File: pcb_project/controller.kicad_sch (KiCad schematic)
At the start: 4 parts, among them U3 COM-09032, U4 COM-09032

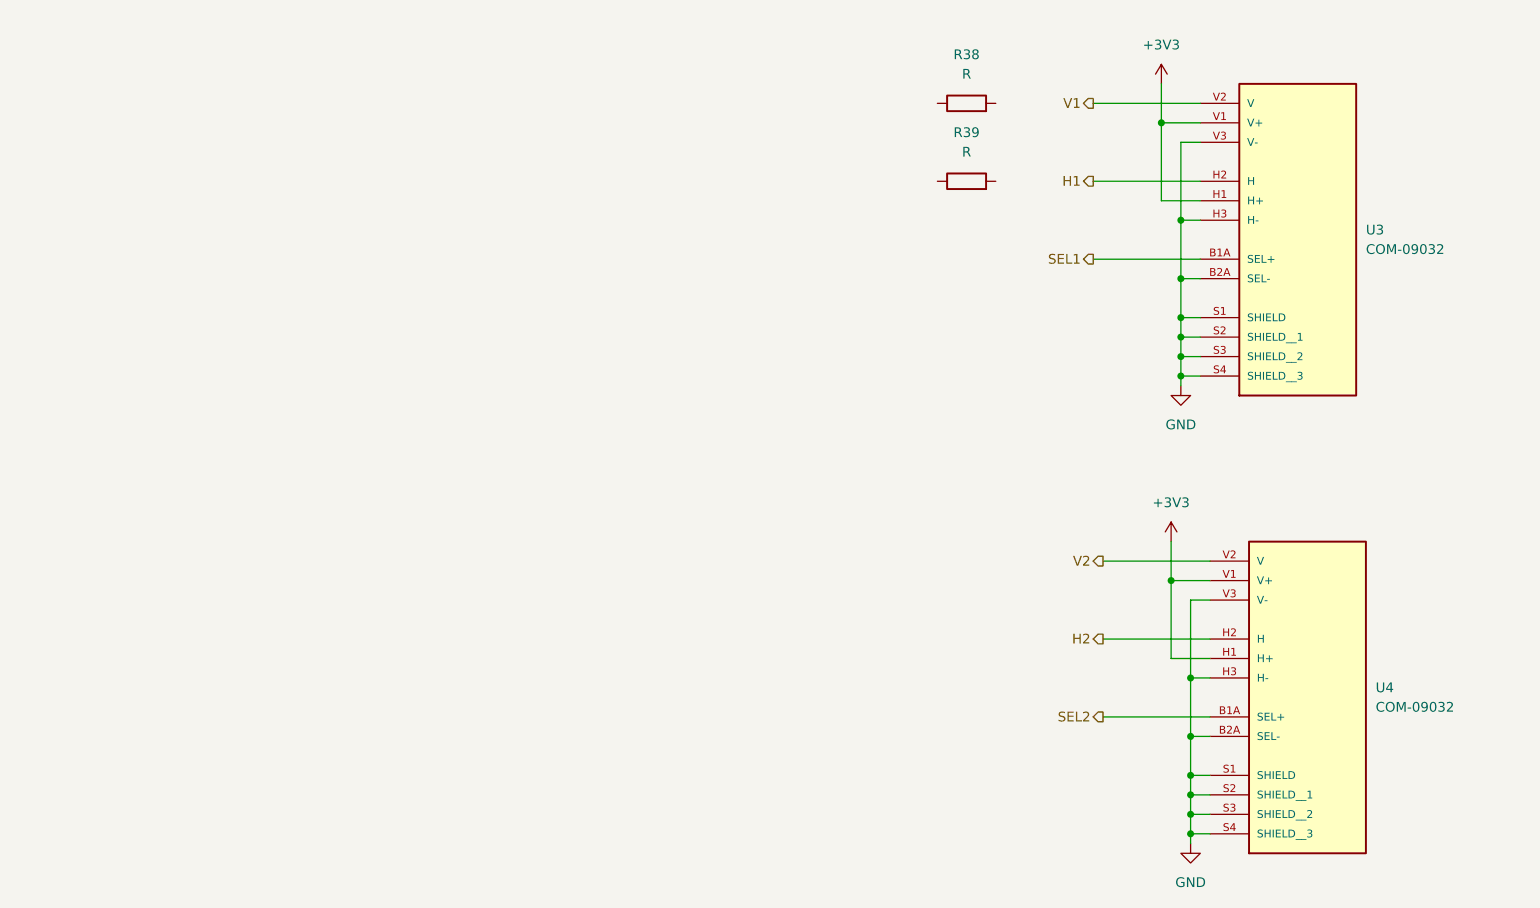
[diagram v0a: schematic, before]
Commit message: Add button symbol
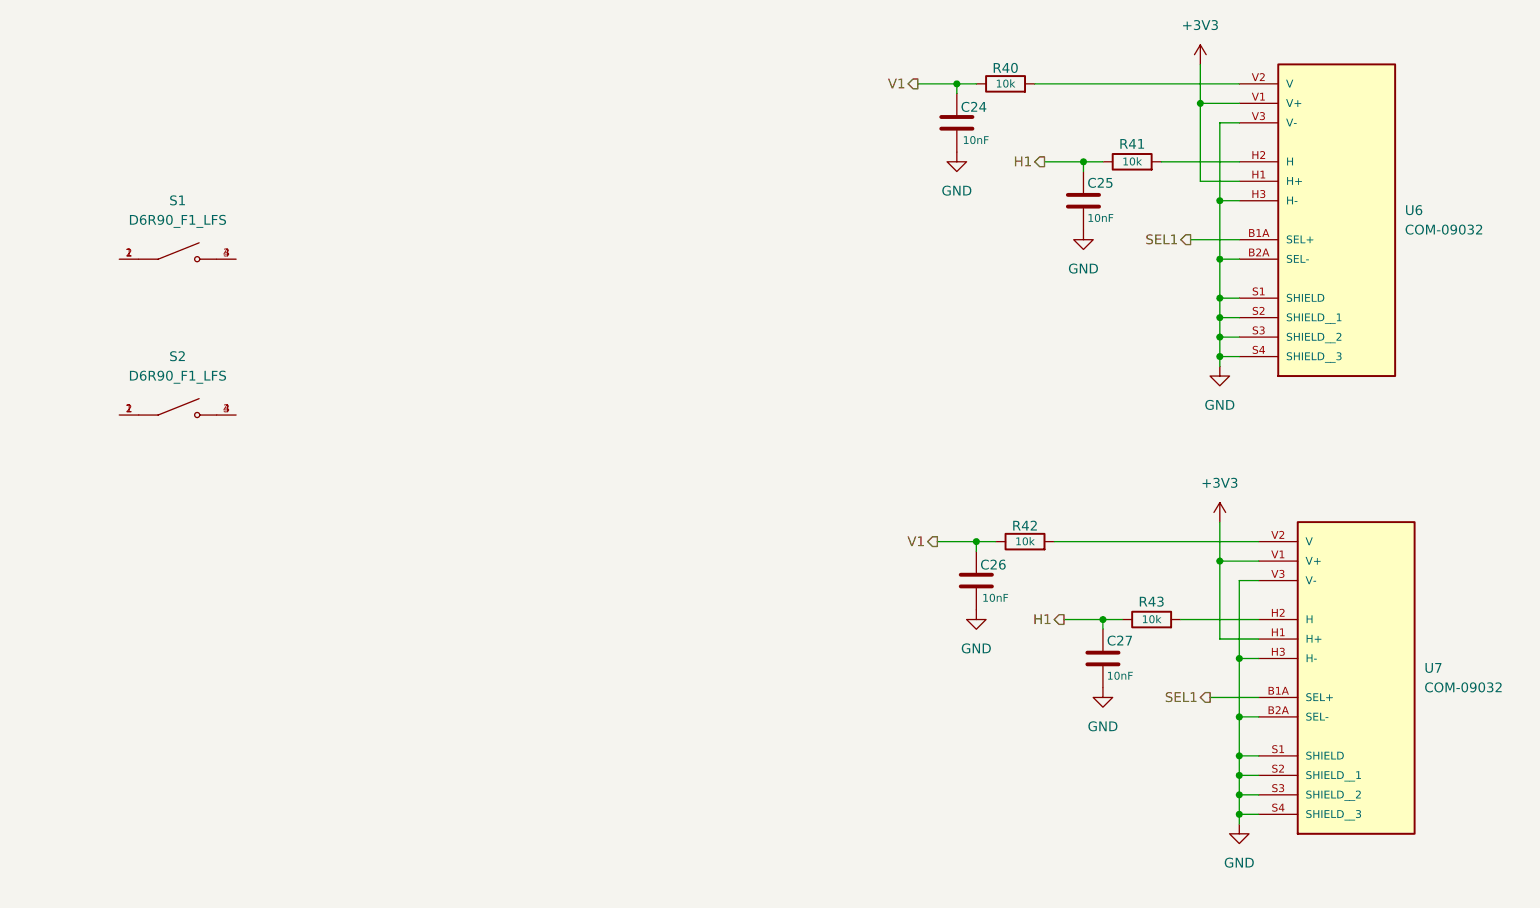
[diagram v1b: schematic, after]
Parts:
- removed R38, R39: R, symbol Device:R
- removed U3, U4: COM-09032, COM-09032:XDCR_COM-09032, symbol COM-09032:COM-09032
- added C24, C25, C26, C27: 10nF, symbol Device:C
- added R40, R41, R42, R43: 10k, symbol Device:R
- added S1, S2: D6R90_F1_LFS, D6R90_F1_LFS:SW_D6R90_F1_LFS, symbol D6R90_F1_LFS:D6R90_F1_LFS
- added U6, U7: COM-09032, COM-09032:XDCR_COM-09032, symbol COM-09032:COM-09032
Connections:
- net +3V3: now also U6.H1 (H+), U6.V1 (V+), U7.H1 (H+), U7.V1 (V+)
- net GND: now also C24.2, C25.2, C26.2, C27.2, U6.B2A (SEL-), U6.H3 (H-), U6.S1 (SHIELD), U6.S2 (SHIELD__1), U6.S3 (SHIELD__2), U6.S4 (SHIELD__3), U6.V3 (V-), U7.B2A (SEL-), U7.H3 (H-), U7.S1 (SHIELD), U7.S2 (SHIELD__1), U7.S3 (SHIELD__2), U7.S4 (SHIELD__3), U7.V3 (V-)
- net H1: now also C25.1, C27.1, R41.1, R43.1
- net SEL1: now also U6.B1A (SEL+), U7.B1A (SEL+)
- net V1: now also C24.1, C26.1, R40.1, R42.1
- new net: R41.2, U6.H2 (H)
- new net: R40.2, U6.V2 (V)
- new net: S2.1, S2.2
- new net: S2.3, S2.4
- new net: R43.2, U7.H2 (H)
- new net: R42.2, U7.V2 (V)
- new net: S1.1, S1.2
- new net: S1.3, S1.4

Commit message: Finish controller schema
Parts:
- removed U7: COM-09032, COM-09032:XDCR_COM-09032, symbol COM-09032:COM-09032
- added R38, R39, R44, R45: 10k, symbol Device:R
- added U3: COM-09032, COM-09032:XDCR_COM-09032, symbol COM-09032:COM-09032
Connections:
- net +3V3: now also R38.1, R39.1, R44.1, R45.1, U3.H1 (H+), U3.V1 (V+)
- net GND: now also S1.1, S1.2, S2.1, S2.2, U3.B2A (SEL-), U3.H3 (H-), U3.S1 (SHIELD), U3.S2 (SHIELD__1), U3.S3 (SHIELD__2), U3.S4 (SHIELD__3), U3.V3 (V-)
- net H1: no longer C27.1, R43.1
- net SEL1: now also R44.2
- net V1: no longer C26.1, R42.1
- net B2: now reaches S2.3, S2.4
- net B2: now also R39.2
- net at R43.2: now also U3.H2 (H)
- net at R42.2: now also U3.V2 (V)
- net B1: now reaches S1.3, S1.4
- net B1: now also R38.2
- new net H2: C27.1, R43.1
- new net SEL2: R45.2, U3.B1A (SEL+)
- new net V2: C26.1, R42.1
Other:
- moved on the sheet: C24, C25, R40, R41, S1, U6

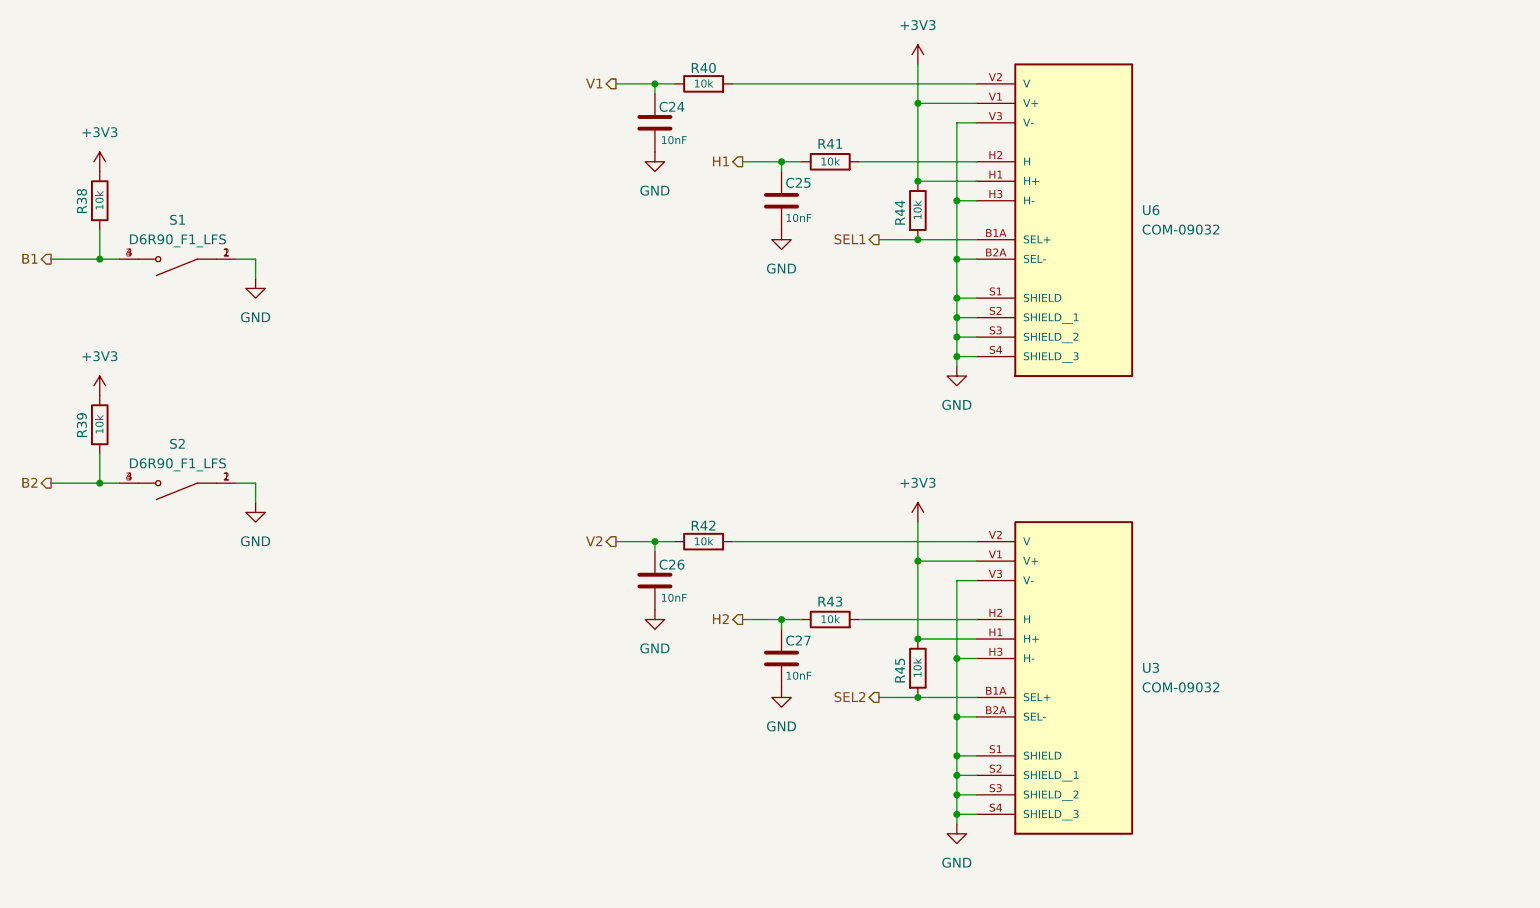
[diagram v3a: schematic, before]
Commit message: ERC fixes, some remain
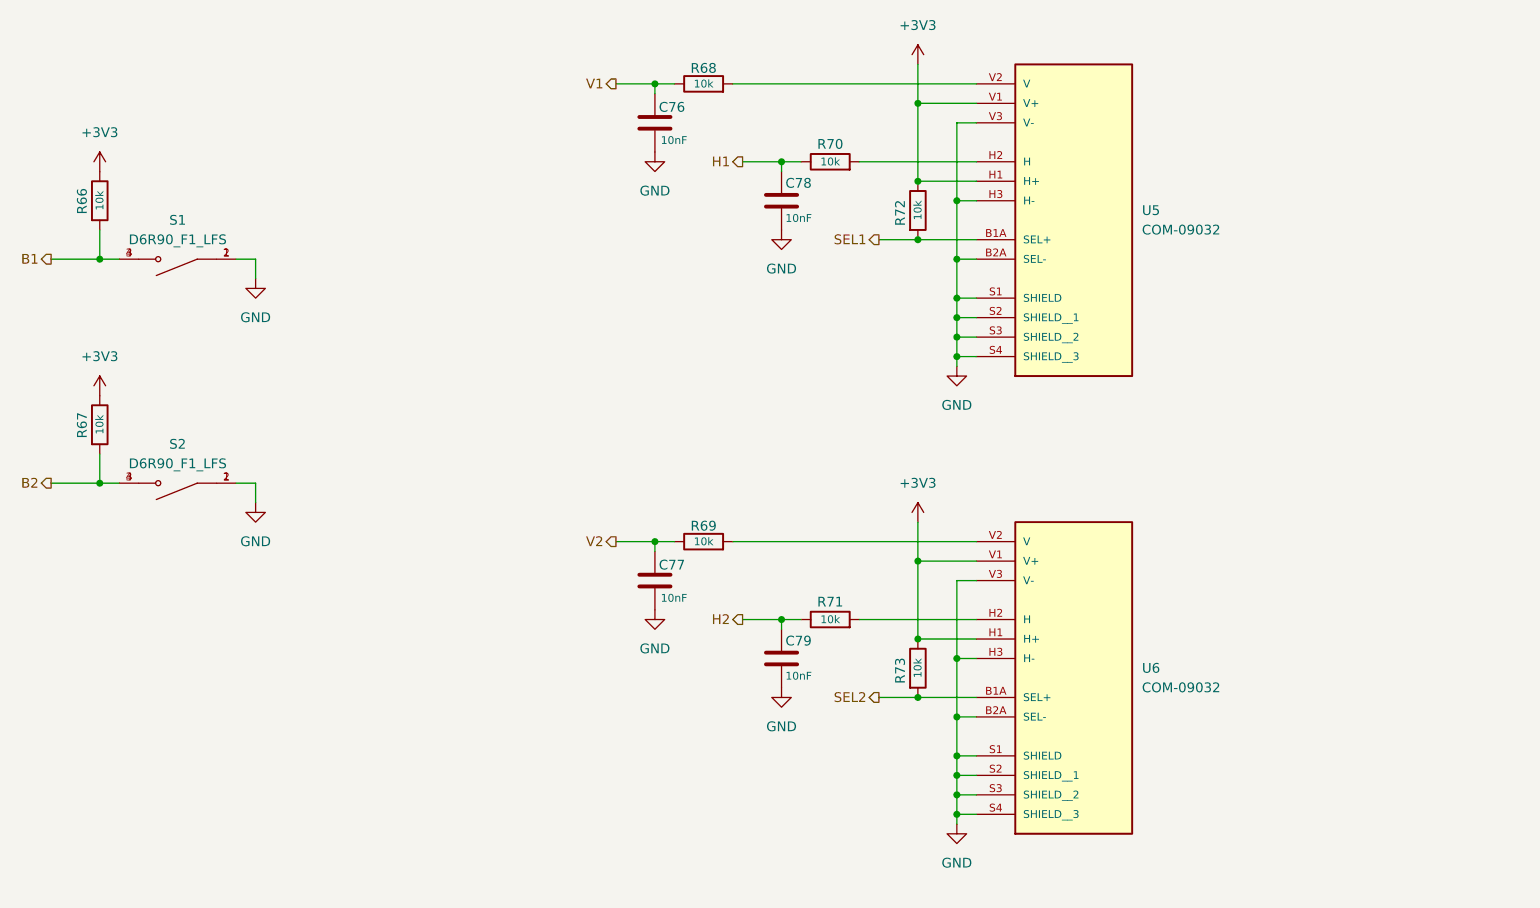
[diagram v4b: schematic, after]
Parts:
- renumbered C24 to C76, C26 to C77, C25 to C78, C27 to C79, R38 to R66, R39 to R67, R40 to R68, R42 to R69, R41 to R70, R43 to R71, R44 to R72, R45 to R73, U6 to U5, U3 to U6
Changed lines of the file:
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@@
 		(dnp no)
 		(fields_autoplaced yes)
-		(property "Reference" "#PWR018"
+		(property "Reference" "#PWR085"
 			(at 82.55 55.88 0)
 			(effects
@@
 			(project ""
 				(path "/98f80f66-4595-4d0f-90ca-59b2db6f447b/8d37cb1b-68e3-4c4f-bec3-1efbc6c7e4dc"
-					(reference "#PWR018")
+					(reference "#PWR085")
 					(unit 1)
 				)
@@
 		(on_board yes)
 		(dnp no)
-		(property "Reference" "R43"
+		(property "Reference" "R71"
 			(at 177.8 108.204 90)
 			(effects
@@
 			(project "pcb_project"
 				(path "/98f80f66-4595-4d0f-90ca-59b2db6f447b/8d37cb1b-68e3-4c4f-bec3-1efbc6c7e4dc"
-					(reference "R43")
+					(reference "R71")
 					(unit 1)
 				)
@@
 		(on_board yes)
 		(dnp no)
-		(property "Reference" "U6"
+		(property "Reference" "U5"
 			(at 218.44 57.1499 0)
 			(effects
@@
 			(project "pcb_project"
 				(path "/98f80f66-4595-4d0f-90ca-59b2db6f447b/8d37cb1b-68e3-4c4f-bec3-1efbc6c7e4dc"
-					(reference "U6")
+					(reference "U5")
 					(unit 1)
 				)
@@
 		(dnp no)
 		(fields_autoplaced yes)
-		(property "Reference" "#PWR016"
+		(property "Reference" "#PWR087"
 			(at 102.87 72.39 0)
 			(effects
@@
 			(project ""
 				(path "/98f80f66-4595-4d0f-90ca-59b2db6f447b/8d37cb1b-68e3-4c4f-bec3-1efbc6c7e4dc"
-					(reference "#PWR016")
+					(reference "#PWR087")
 					(unit 1)
 				)
@@
 		(on_board yes)
 		(dnp no)
-		(property "Reference" "U3"
+		(property "Reference" "U6"
 			(at 218.44 116.8399 0)
 			(effects
@@
 			(project "pcb_project"
 				(path "/98f80f66-4595-4d0f-90ca-59b2db6f447b/8d37cb1b-68e3-4c4f-bec3-1efbc6c7e4dc"
-					(reference "U3")
+					(reference "U6")
 					(unit 1)
 				)
@@
 		(dnp no)
 		(fields_autoplaced yes)
-		(property "Reference" "#PWR025"
+		(property "Reference" "#PWR094"
 			(at 189.23 101.6 0)
 			(effects
@@
 			(project "pcb_project"
 				(path "/98f80f66-4595-4d0f-90ca-59b2db6f447b/8d37cb1b-68e3-4c4f-bec3-1efbc6c7e4dc"
-					(reference "#PWR025")
+					(reference "#PWR094")
 					(unit 1)
 				)
@@
 		(dnp no)
 		(fields_autoplaced yes)
-		(property "Reference" "#PWR0110"
+		(property "Reference" "#PWR092"
 			(at 171.45 125.73 0)
 			(effects
@@
 			(project "pcb_project"
 				(path "/98f80f66-4595-4d0f-90ca-59b2db6f447b/8d37cb1b-68e3-4c4f-bec3-1efbc6c7e4dc"
-					(reference "#PWR0110")
+					(reference "#PWR092")
 					(unit 1)
 				)
@@
 		(dnp no)
 		(fields_autoplaced yes)
-		(property "Reference" "#PWR022"
+		(property "Reference" "#PWR095"
 			(at 194.31 83.82 0)
 			(effects
@@
 			(project "pcb_project"
 				(path "/98f80f66-4595-4d0f-90ca-59b2db6f447b/8d37cb1b-68e3-4c4f-bec3-1efbc6c7e4dc"
-					(reference "#PWR022")
+					(reference "#PWR095")
 					(unit 1)
 				)
@@
 		(on_board yes)
 		(dnp no)
-		(property "Reference" "R42"
+		(property "Reference" "R69"
 			(at 161.29 98.298 90)
 			(effects
@@
 			(project "pcb_project"
 				(path "/98f80f66-4595-4d0f-90ca-59b2db6f447b/8d37cb1b-68e3-4c4f-bec3-1efbc6c7e4dc"
-					(reference "R42")
+					(reference "R69")
 					(unit 1)
 				)
@@
 		(on_board yes)
 		(dnp no)
-		(property "Reference" "R38"
+		(property "Reference" "R66"
 			(at 80.264 57.658 90)
 			(effects
@@
 			(project ""
 				(path "/98f80f66-4595-4d0f-90ca-59b2db6f447b/8d37cb1b-68e3-4c4f-bec3-1efbc6c7e4dc"
-					(reference "R38")
+					(reference "R66")
 					(unit 1)
 				)
@@
 		(dnp no)
 		(fields_autoplaced yes)
-		(property "Reference" "#PWR020"
+		(property "Reference" "#PWR088"
 			(at 102.87 101.6 0)
 			(effects
@@
 			(project "pcb_project"
 				(path "/98f80f66-4595-4d0f-90ca-59b2db6f447b/8d37cb1b-68e3-4c4f-bec3-1efbc6c7e4dc"
-					(reference "#PWR020")
+					(reference "#PWR088")
 					(unit 1)
 				)
@@
 		(dnp no)
 		(fields_autoplaced yes)
-		(property "Reference" "#PWR0103"
+		(property "Reference" "#PWR089"
 			(at 154.94 55.88 0)
 			(effects
@@
 			(project "pcb_project"
 				(path "/98f80f66-4595-4d0f-90ca-59b2db6f447b/8d37cb1b-68e3-4c4f-bec3-1efbc6c7e4dc"
-					(reference "#PWR0103")
+					(reference "#PWR089")
 					(unit 1)
 				)
@@
 		(on_board yes)
 		(dnp no)
-		(property "Reference" "C27"
+		(property "Reference" "C79"
 			(at 171.958 113.284 0)
 			(effects
@@
 			(project "pcb_project"
 				(path "/98f80f66-4595-4d0f-90ca-59b2db6f447b/8d37cb1b-68e3-4c4f-bec3-1efbc6c7e4dc"
-					(reference "C27")
+					(reference "C79")
 					(unit 1)
 				)
@@
 		(dnp no)
 		(fields_autoplaced yes)
-		(property "Reference" "#PWR021"
+		(property "Reference" "#PWR093"
 			(at 189.23 41.91 0)
 			(effects
@@
 			(project "pcb_project"
 				(path "/98f80f66-4595-4d0f-90ca-59b2db6f447b/8d37cb1b-68e3-4c4f-bec3-1efbc6c7e4dc"
-					(reference "#PWR021")
+					(reference "#PWR093")
 					(unit 1)
 				)
@@
 		(on_board yes)
 		(dnp no)
-		(property "Reference" "R44"
+		(property "Reference" "R72"
 			(at 186.944 59.182 90)
 			(effects
@@
 			(project ""
 				(path "/98f80f66-4595-4d0f-90ca-59b2db6f447b/8d37cb1b-68e3-4c4f-bec3-1efbc6c7e4dc"
-					(reference "R44")
+					(reference "R72")
 					(unit 1)
 				)
@@
 		(on_board yes)
 		(dnp no)
-		(property "Reference" "C24"
+		(property "Reference" "C76"
 			(at 155.448 43.688 0)
 			(effects
@@
 			(project "pcb_project"
 				(path "/98f80f66-4595-4d0f-90ca-59b2db6f447b/8d37cb1b-68e3-4c4f-bec3-1efbc6c7e4dc"
-					(reference "C24")
+					(reference "C76")
 					(unit 1)
 				)
@@
 		(on_board yes)
 		(dnp no)
-		(property "Reference" "C26"
+		(property "Reference" "C77"
 			(at 155.448 103.378 0)
 			(effects
@@
 			(project "pcb_project"
 				(path "/98f80f66-4595-4d0f-90ca-59b2db6f447b/8d37cb1b-68e3-4c4f-bec3-1efbc6c7e4dc"
-					(reference "C26")
+					(reference "C77")
 					(unit 1)
 				)
@@
 		(on_board yes)
 		(dnp no)
-		(property "Reference" "R39"
+		(property "Reference" "R67"
 			(at 80.264 86.868 90)
 			(effects
@@
 			(project "pcb_project"
 				(path "/98f80f66-4595-4d0f-90ca-59b2db6f447b/8d37cb1b-68e3-4c4f-bec3-1efbc6c7e4dc"
-					(reference "R39")
+					(reference "R67")
 					(unit 1)
 				)
@@
 		(dnp no)
 		(fields_autoplaced yes)
-		(property "Reference" "#PWR019"
+		(property "Reference" "#PWR086"
 			(at 82.55 85.09 0)
 			(effects
@@
 			(project "pcb_project"
 				(path "/98f80f66-4595-4d0f-90ca-59b2db6f447b/8d37cb1b-68e3-4c4f-bec3-1efbc6c7e4dc"
-					(reference "#PWR019")
+					(reference "#PWR086")
 					(unit 1)
 				)
@@
 		(on_board yes)
 		(dnp no)
-		(property "Reference" "C25"
+		(property "Reference" "C78"
 			(at 171.958 53.594 0)
 			(effects
@@
 			(project "pcb_project"
 				(path "/98f80f66-4595-4d0f-90ca-59b2db6f447b/8d37cb1b-68e3-4c4f-bec3-1efbc6c7e4dc"
-					(reference "C25")
+					(reference "C78")
 					(unit 1)
 				)
@@
 		(dnp no)
 		(fields_autoplaced yes)
-		(property "Reference" "#PWR0104"
+		(property "Reference" "#PWR091"
 			(at 171.45 66.04 0)
 			(effects
@@
 			(project "pcb_project"
 				(path "/98f80f66-4595-4d0f-90ca-59b2db6f447b/8d37cb1b-68e3-4c4f-bec3-1efbc6c7e4dc"
-					(reference "#PWR0104")
+					(reference "#PWR091")
 					(unit 1)
 				)
@@
 		(dnp no)
 		(fields_autoplaced yes)
-		(property "Reference" "#PWR026"
+		(property "Reference" "#PWR096"
 			(at 194.31 143.51 0)
 			(effects
@@
 			(project "pcb_project"
 				(path "/98f80f66-4595-4d0f-90ca-59b2db6f447b/8d37cb1b-68e3-4c4f-bec3-1efbc6c7e4dc"
-					(reference "#PWR026")
+					(reference "#PWR096")
 					(unit 1)
 				)
@@
 		(dnp no)
 		(fields_autoplaced yes)
-		(property "Reference" "#PWR023"
+		(property "Reference" "#PWR090"
 			(at 154.94 115.57 0)
 			(effects
@@
 			(project "pcb_project"
 				(path "/98f80f66-4595-4d0f-90ca-59b2db6f447b/8d37cb1b-68e3-4c4f-bec3-1efbc6c7e4dc"
-					(reference "#PWR023")
+					(reference "#PWR090")
 					(unit 1)
 				)
@@
 		(on_board yes)
 		(dnp no)
-		(property "Reference" "R40"
+		(property "Reference" "R68"
 			(at 161.29 38.608 90)
 			(effects
@@
 			(project "pcb_project"
 				(path "/98f80f66-4595-4d0f-90ca-59b2db6f447b/8d37cb1b-68e3-4c4f-bec3-1efbc6c7e4dc"
-					(reference "R40")
+					(reference "R68")
 					(unit 1)
 				)
@@
 		(on_board yes)
 		(dnp no)
-		(property "Reference" "R45"
+		(property "Reference" "R73"
 			(at 186.944 118.872 90)
 			(effects
@@
 			(project "pcb_project"
 				(path "/98f80f66-4595-4d0f-90ca-59b2db6f447b/8d37cb1b-68e3-4c4f-bec3-1efbc6c7e4dc"
-					(reference "R45")
+					(reference "R73")
 					(unit 1)
 				)
@@
 		(on_board yes)
 		(dnp no)
-		(property "Reference" "R41"
+		(property "Reference" "R70"
 			(at 177.8 48.514 90)
 			(effects
@@
 			(project "pcb_project"
 				(path "/98f80f66-4595-4d0f-90ca-59b2db6f447b/8d37cb1b-68e3-4c4f-bec3-1efbc6c7e4dc"
-					(reference "R41")
-					(unit 1)
-				)
+					(reference "R70")
+					(unit 1)
+				)
